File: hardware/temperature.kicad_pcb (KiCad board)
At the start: 2 copper layers, 15 x 25 mm, 23 parts, among them P1 CON-SENSOR2, P2 DEBUG, P3 BOOT, U1 XMC1XXX24, U2 TMP102, U3 DRILL, U4 DRILL, U5 DRILL, U6 DRILL

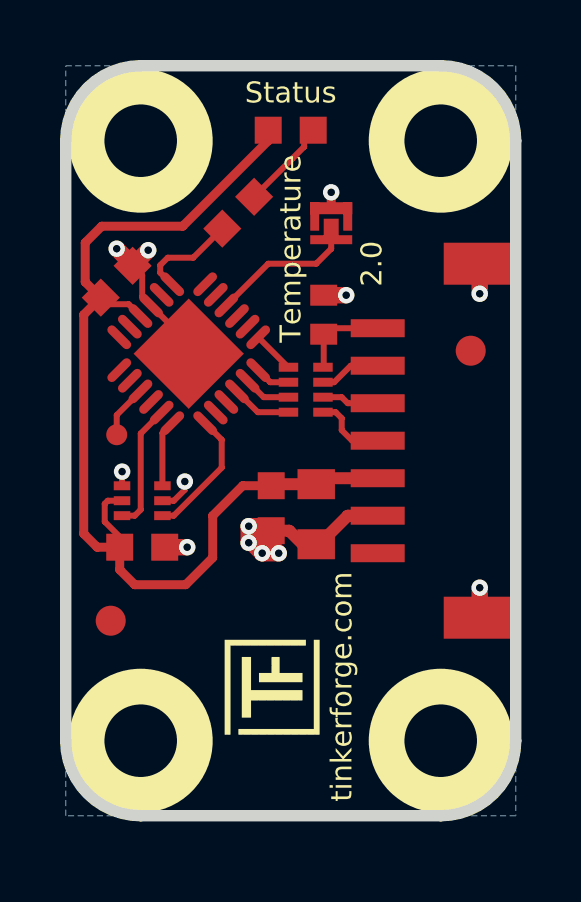
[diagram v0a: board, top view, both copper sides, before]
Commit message: change sensor to SHT3X Sensirion
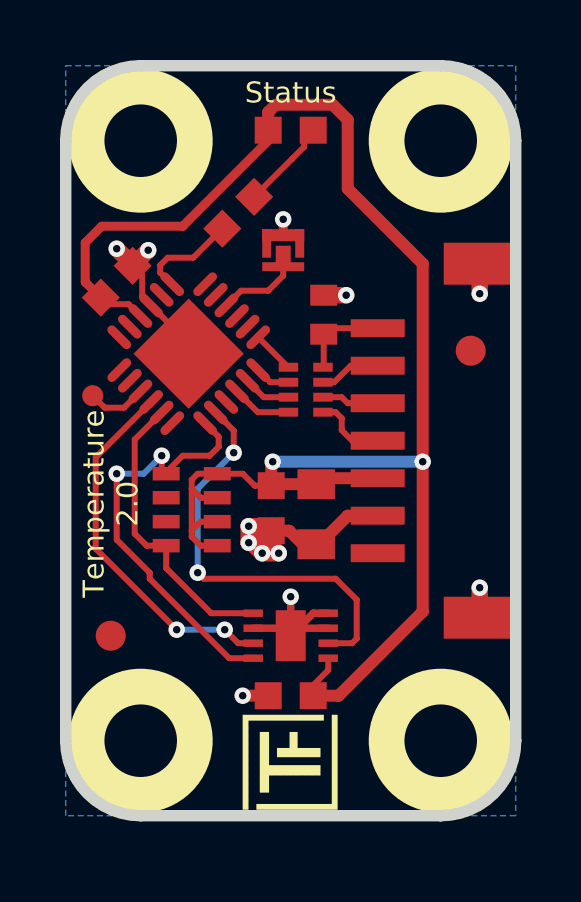
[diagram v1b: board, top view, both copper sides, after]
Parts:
- added RP2: 1k, kicad-libraries:4X0603, F.Cu at (144.5, 105.4)
- U2: value TMP102 -> STS3x-DIS; footprint kicad-libraries:SOT563 -> SHT3x-DIS
- moved VAL 15.1 mm to (147.8, 110.6)
- moved G*** 15.1 mm to (147.8, 95.6)
- moved C2 7.00 mm to (147.8, 111.6)
- moved U2 6.69 mm to (147.8, 109.6), turned to 0 degrees
- moved Ref** 2.57 mm to (146.2, 115.4)
- moved P3 1.84 mm to (147.6, 96.8)
- moved P2 1.53 mm to (141.2, 101.6)
- moved Fiducial_Mark 0.50 mm to (141.8, 109.6)
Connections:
- C2 pad 1: VCC -> GND
- C2 pad 2: GND -> VCC
- P1 pad 1: Net-(P1-Pad1) -> (no net)
- U1 pad 11: Net-(U1-Pad11) -> (no net)
- U1 pad 12: Net-(U1-Pad12) -> (no net)
- U1 pad 13: Net-(U1-Pad13) -> (no net)
- U1 pad 14: Net-(U1-Pad14) -> (no net)
- U1 pad 16: Net-(U1-Pad16) -> ALERT
- U1 pad 18: ALERT -> (no net)
- U1 pad 2: Net-(U1-Pad2) -> (no net)
- U1 pad 20: Net-(U1-Pad20) -> RESET
- U1 pad 21: Net-(U1-Pad21) -> (no net)
- U1 pad 3: Net-(U1-Pad3) -> (no net)
- U1 pad 5: Net-(U1-Pad5) -> (no net)
- U1 pad 6: Net-(U1-Pad6) -> (no net)
- U1 pad 8: Net-(U1-Pad8) -> (no net)
- U2 pad 1: SCL -> SDA
- U2 pad 4: GND -> SCL
- U2 pad 6: SDA -> RESET
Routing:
- net VCC: track 35.1 -> 55.9 mm, vias 0 -> 2
- net RESET: track 0.00 -> 14.1 mm, vias 0 -> 2
- net ALERT: track 2.22 -> 12.2 mm, vias 0 -> 2
- net SCL: track 4.35 -> 14.0 mm, vias 0 -> 2
- net SDA: track 4.23 -> 9.90 mm
- net GND: track 26.8 -> 30.8 mm, vias 13 -> 12
- net Net-(P3-Pad2): track 4.98 -> 3.41 mm
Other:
- board text added: "Temperature 2.0"
- board text removed: "2.0"
- board text removed: "Temperature"

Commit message: remove alert pin connection
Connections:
- U1 pad 16: ALERT -> (no net)
- U2 pad 3: ALERT -> (no net)
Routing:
- net ALERT: track 12.2 -> 0.00 mm, vias 2 -> 0
